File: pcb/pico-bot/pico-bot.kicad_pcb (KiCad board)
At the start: 2 copper layers, 101.6 x 54.6 mm, 62 parts, among them J1 Conn_01x02_Male, J2 Conn_01x06_Male, J3 Conn_01x06_Male, J4 Conn_01x06_Male, J5 Conn_01x06_Male, Q1 DMG2305UX, Q2 AOD417, SW1 SW_SPDT, SW2 SW_Push, SW3 SW_Push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

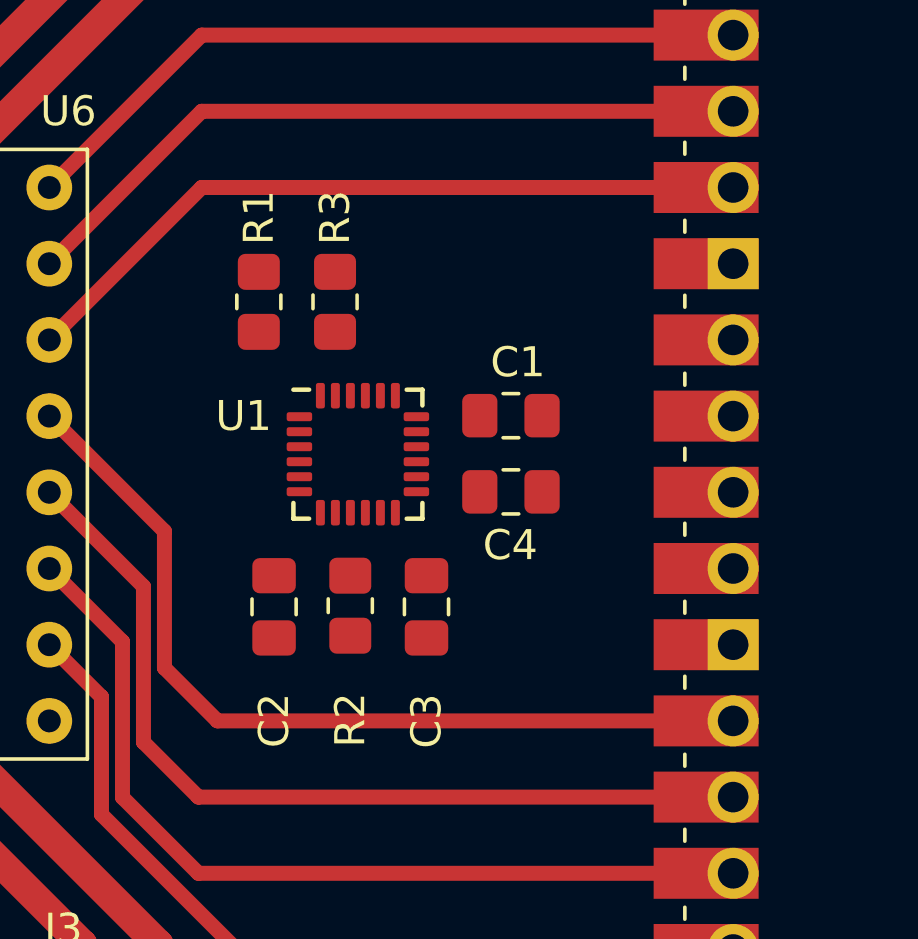
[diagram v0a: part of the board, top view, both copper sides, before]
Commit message: Center and route MPU-6050
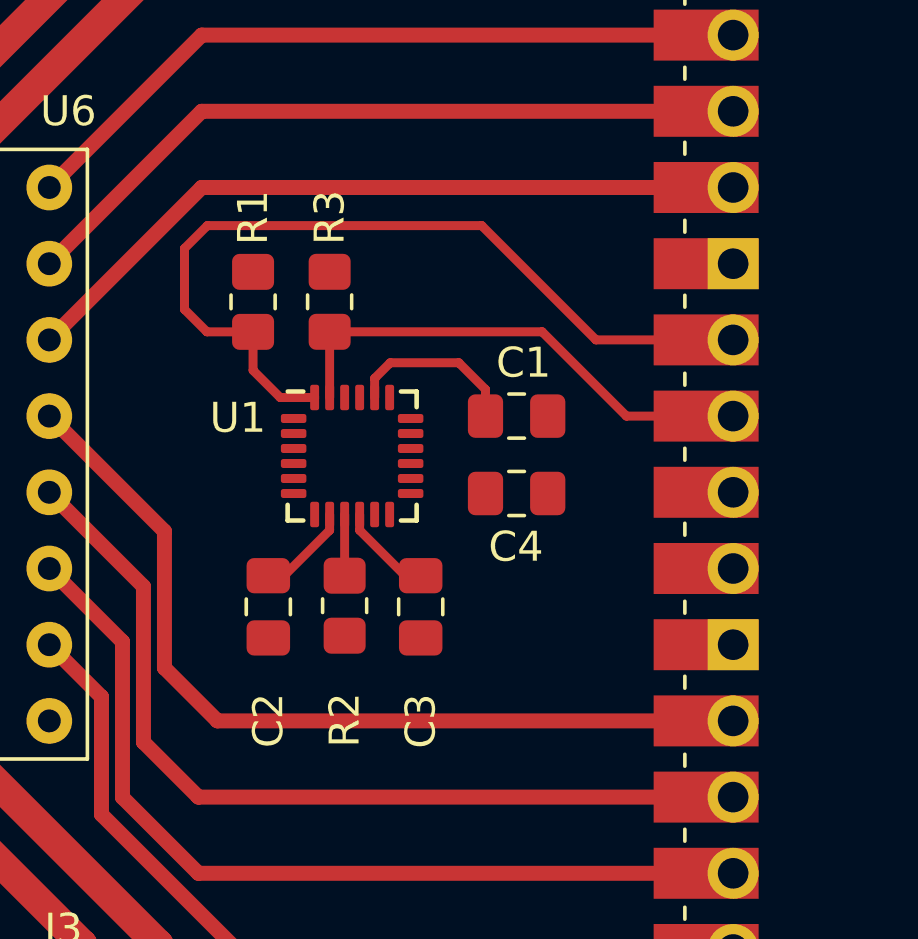
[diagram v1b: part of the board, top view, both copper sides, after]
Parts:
- moved U1 0.20 mm to (147.9, 93.8)
- moved C4 0.20 mm to (153.4, 95.0)
- moved C2 0.19 mm to (145.1, 98.8)
- moved C3 0.19 mm to (150.2, 98.8)
- moved R1 0.19 mm to (144.6, 88.7)
- moved C1 0.19 mm to (153.4, 92.5)
- moved R2 0.19 mm to (147.6, 98.8)
- moved R3 0.18 mm to (147.1, 88.7)
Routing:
- net /SDA: track 0.00 -> 28.5 mm
- net /SCL: track 0.02 -> 16.8 mm
- net Net-(C1-Pad2): track 0.00 -> 5.81 mm
- net +3V3: track 0.00 -> 3.20 mm
- net Net-(C3-Pad2): track 0.00 -> 3.19 mm
- net Net-(R2-Pad2): track 0.01 -> 2.04 mm

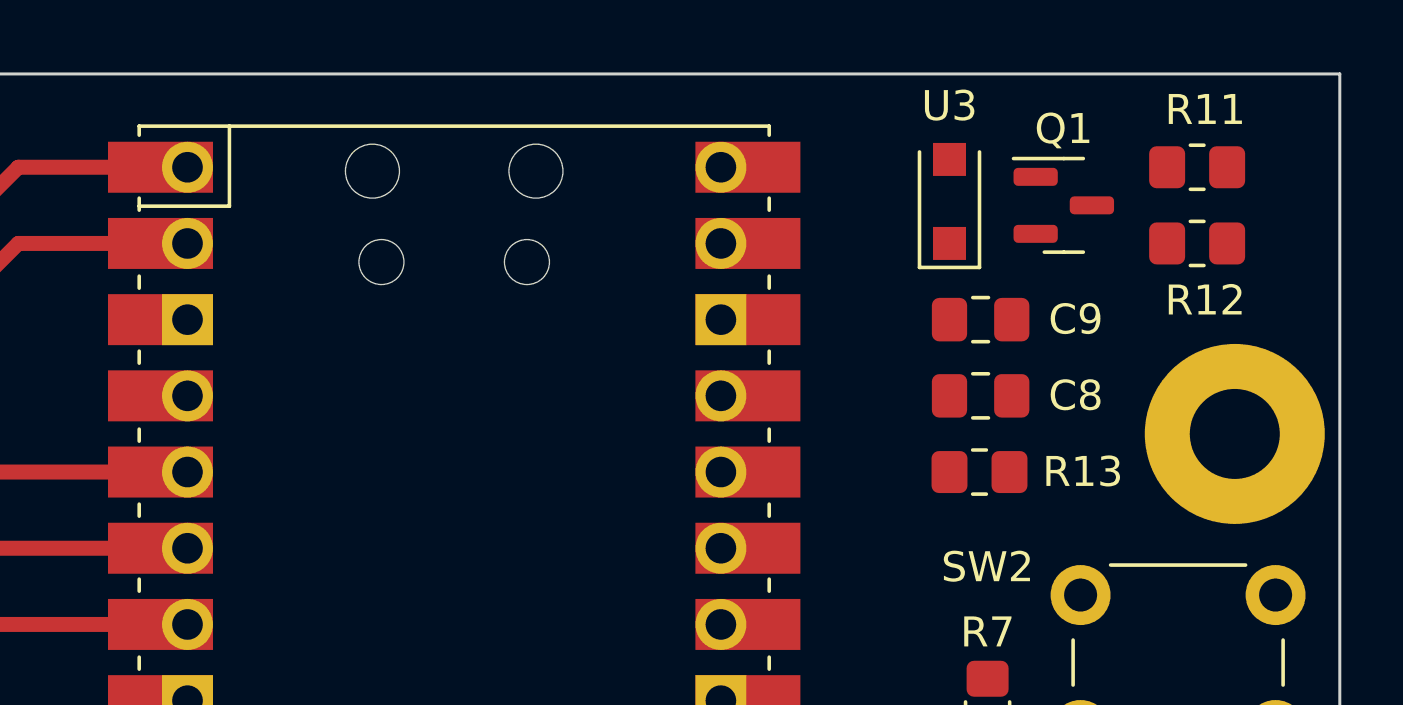
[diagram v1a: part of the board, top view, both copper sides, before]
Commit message: Route pico power select circuit
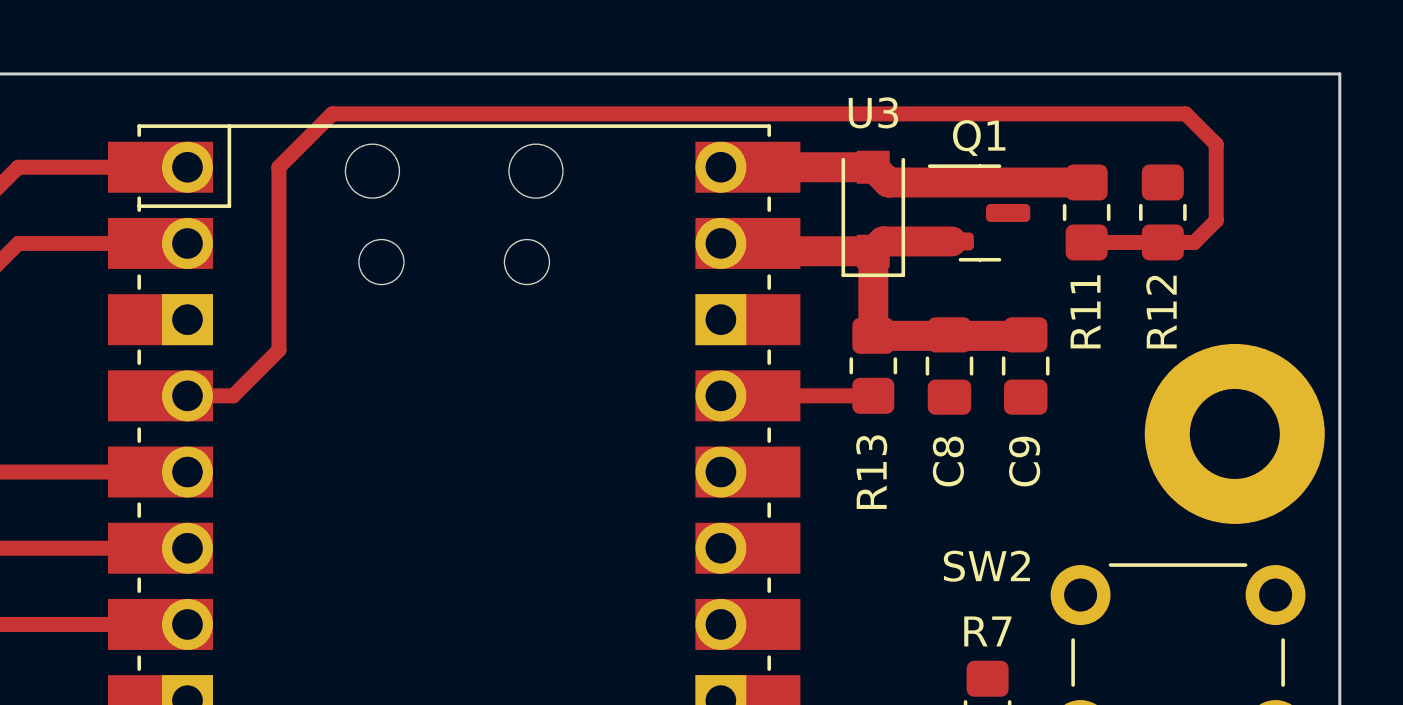
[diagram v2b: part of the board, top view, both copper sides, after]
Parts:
- moved R13 5.01 mm to (183.4, 76.2), turned to 90 degrees
- moved R11 3.98 mm to (190.6, 71.1), turned to 90 degrees
- moved Q1 2.81 mm to (187.0, 71.1)
- moved U3 2.55 mm to (183.4, 71.0)
- moved C9 2.16 mm to (188.5, 76.2), turned to 90 degrees
- moved R12 1.54 mm to (193.1, 71.1), turned to -90 degrees
- moved C8 1.44 mm to (186.0, 76.2), turned to 90 degrees
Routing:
- net /VBUS_IN: track 0.00 -> 49.3 mm
- net VSYS: track 0.00 -> 15.9 mm
- net VBUS: track 0.00 -> 12.4 mm
- net /3V3_EN: track 0.00 -> 5.08 mm

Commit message: Route all except power and ground
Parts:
- removed J5: Conn_01x06_Male, Connector_PinHeader_2.54mm:PinHeader_2x03_P2.54mm_Vertical
- J4: value Conn_01x06_Male -> Conn_01x08_Male; footprint Connector_PinHeader_2.54mm:PinHeader_2x03_P2.54mm_Vertical -> Connector_PinHeader_2.54mm:PinHeader_2x04_P2.54mm_Vertical
- R4: value 220R -> 10k
- R7: value 10k -> 220R
- moved R4 19.0 mm to (187.3, 85.8), turned to -90 degrees
- moved R7 15.1 mm to (185.5, 102.6), turned to 180 degrees
- moved SW2 7.91 mm to (196.9, 88.4), turned to 180 degrees
- moved R6 7.82 mm to (185.5, 105.2)
- moved R5 6.94 mm to (185.5, 97.5)
- moved TP1 2.29 mm to (100.9, 71.9)
- moved D1 1.91 mm to (193.6, 101.9), turned to 0 degrees
- moved J4 1.63 mm to (185.7, 110.2), turned to 0 degrees
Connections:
- J4 pad 2: /SPARE1 -> +3V3
- J4 pad 3: /SPARE2 -> /SPARE1
- J4 pad 4: /SPARE3 -> +3V3
- J4 pad 5: /SPARE4 -> /SPARE2
- J4 pad 6: /SPARE5 -> GND
- R4 pad 1: Net-(D1-Pad4) -> /MODE
- R4 pad 2: Net-(R4-Pad2) -> +3V3
- R5 pad 1: Net-(D1-Pad3) -> Net-(D1-Pad4)
- R6 pad 1: Net-(D1-Pad2) -> Net-(D1-Pad3)
- R7 pad 1: /MODE -> Net-(D1-Pad2)
- R7 pad 2: +3V3 -> Net-(R7-Pad2)
- U4 pad 12: /SPARE0 -> unconnected-(U4-Pad12)
- U4 pad 21: /SPARE5 -> /SPARE3
- U4 pad 22: /SPARE4 -> /SPARE2
- U4 pad 24: /SPARE3 -> /SPARE1
- U4 pad 25: /SPARE2 -> /SPARE0
- U4 pad 26: Net-(U4-Pad26) -> Net-(R6-Pad2)
- U4 pad 27: Net-(U4-Pad27) -> Net-(R7-Pad2)
- U4 pad 29: Net-(U4-Pad29) -> Net-(R5-Pad2)
- U4 pad 32: /SPARE1 -> unconnected-(U4-Pad32)
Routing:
- net /RESET: track 0.00 -> 19.7 mm
- net /MODE: track 0.00 -> 18.9 mm
- net Net-(D1-Pad4): track 0.00 -> 10.4 mm
- net Net-(D1-Pad3): track 0.00 -> 9.96 mm
- net /SPARE1: track 0.00 -> 8.42 mm
- net /SPARE0: track 0.00 -> 8.42 mm
- net /SPARE3: track 0.00 -> 7.37 mm
- net /SPARE2: track 0.00 -> 7.37 mm
- net Net-(R7-Pad2): track 0.00 -> 6.10 mm
- net Net-(R6-Pad2): track 0.00 -> 6.10 mm
- net Net-(R5-Pad2): track 0.00 -> 6.10 mm
- net Net-(D1-Pad2): track 0.00 -> 5.39 mm

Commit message: Add pours, pour currently broken
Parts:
- moved D3 23.2 mm to (131.6, 112.3), turned to 90 degrees
- moved R17 22.1 mm to (134.7, 112.3), turned to 90 degrees
- moved R4 4.31 mm to (183.4, 83.8), turned to 90 degrees
- moved R2 3.46 mm to (150.4, 100.9), turned to 180 degrees
- moved C17 1.42 mm to (122.5, 86.4), turned to -90 degrees
- moved C2 1.15 mm to (146.2, 98.7)
- moved J1 1.04 mm to (102.2, 102.4)
- moved C18 0.71 mm to (145.5, 72.4)
- moved C19 0.58 mm to (145.5, 115.3)
- moved C4 0.51 mm to (152.9, 95.0)
- moved R1 0.41 mm to (145.0, 88.8)
- moved C3 0.39 mm to (150.5, 98.6), turned to 180 degrees
- moved C15 0.16 mm to (126.8, 115.6)
- moved R3 0.14 mm to (147.1, 88.8)
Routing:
- net /VBAT_MEASURE: track 0.55 -> 78.1 mm
- net GND: track 0.00 -> 45.2 mm, vias 0 -> 28
- net /INT: track 0.00 -> 12.4 mm
- net VBAT: track 43.1 -> 51.8 mm
- net Net-(R2-Pad2): track 2.04 -> 6.36 mm
- net +3V3: track 3.20 -> 0.00 mm
- net /STDBY: track 29.7 -> 31.4 mm
- net /SDA: track 28.5 -> 27.4 mm
- net Net-(C3-Pad2): track 3.19 -> 3.80 mm
- net /MODE: track 18.9 -> 18.4 mm
- added copper zone on F.Cu, net +3V3
- added copper zone on B.Cu, net GND
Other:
- outline, holes or cut-outs redrawn
- board text added: "+"
- board text added: "-"
- board text added: "MODE"
- board text added: "OFF"
- board text added: "ON"
- board text added: "RESET"

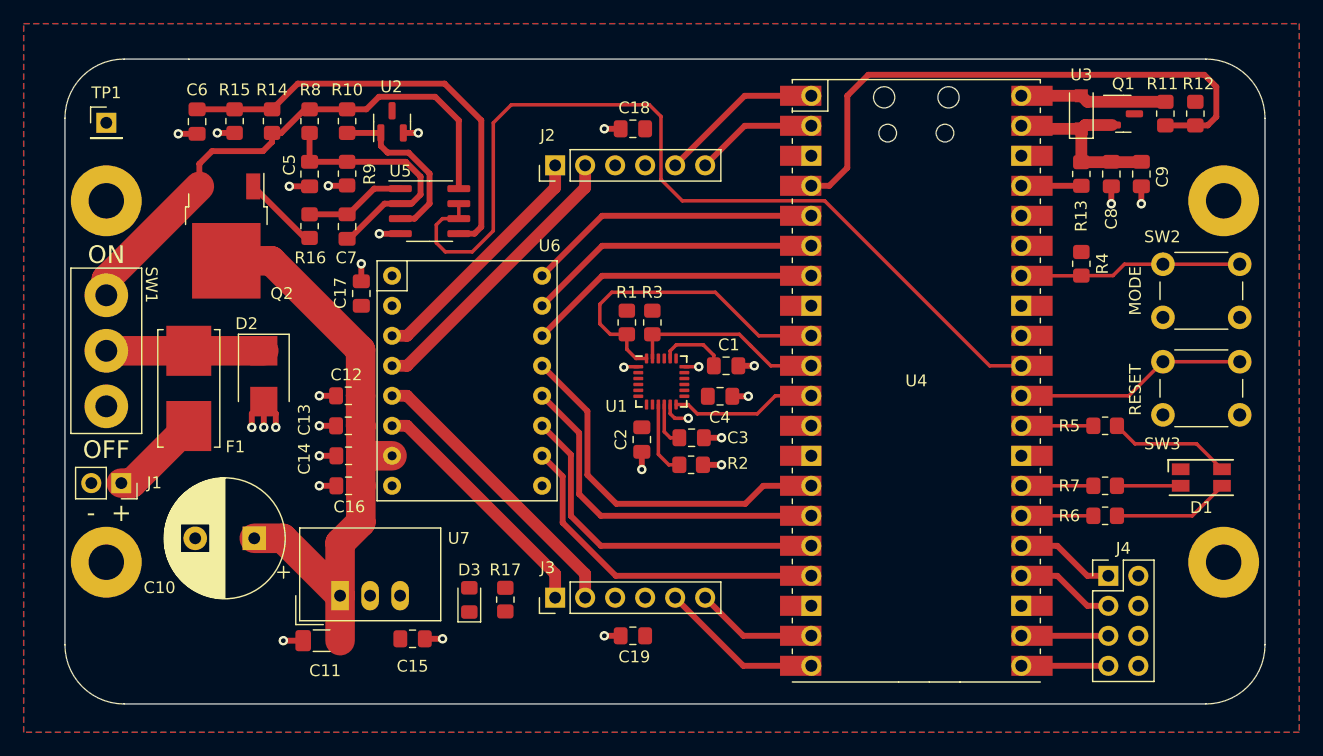
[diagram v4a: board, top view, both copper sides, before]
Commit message: Update pour clearance and repour, now all nets are connected
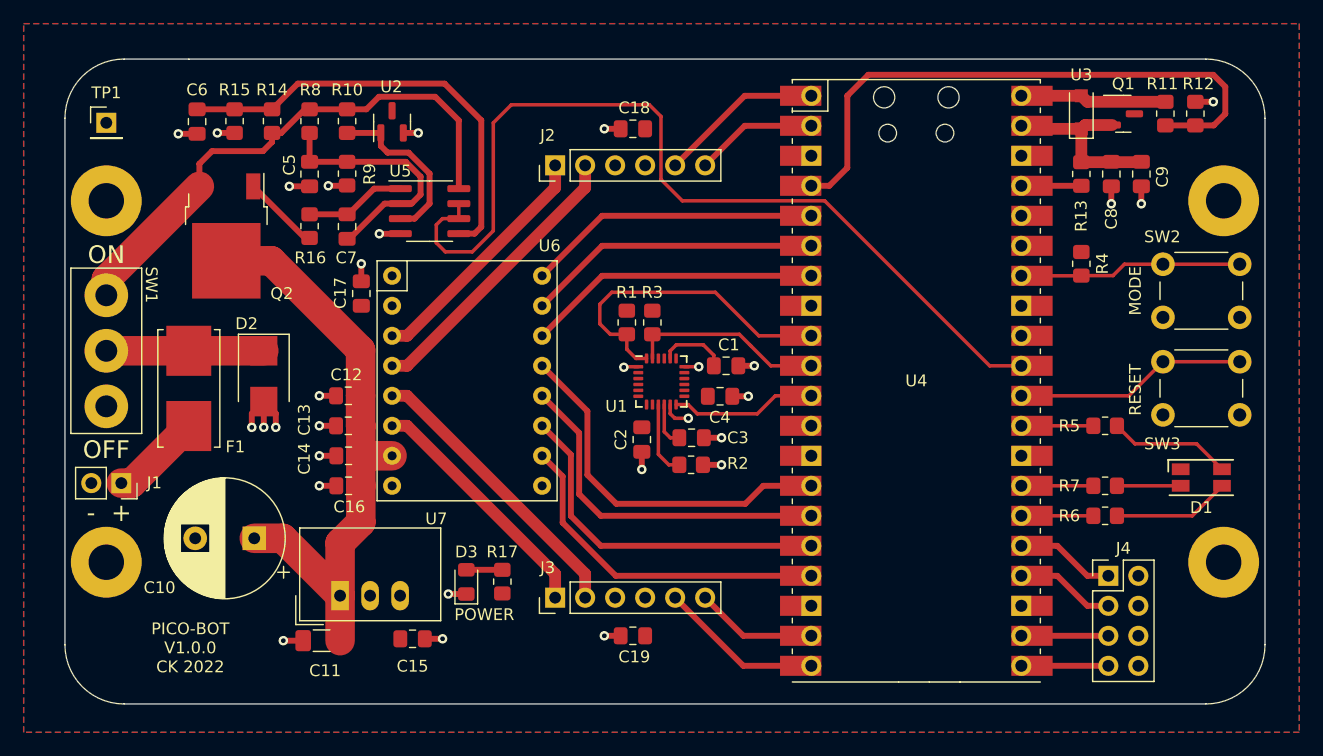
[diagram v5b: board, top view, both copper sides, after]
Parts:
- moved D3 1.55 mm to (131.4, 110.8)
- moved R17 1.55 mm to (134.4, 110.7)
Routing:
- net GND: track 45.2 -> 48.3 mm, vias 28 -> 30
- net Net-(D3-Pad2): track 0.00 -> 3.05 mm
- net /VBUS_IN: track 49.3 -> 50.7 mm
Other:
- board text added: "PICO-BOT V1.0.0 CK 2022"
- board text added: "POWER"

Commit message: Address DRC warnings
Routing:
- net /VBAT_MEASURE: track 78.1 -> 77.6 mm
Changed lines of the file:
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@@
   (segment (start 143.064 72.404) (end 144.445 72.404) (width 0.5) (layer "F.Cu") (net 1))
   (segment (start 119.696 77.23) (end 121.255 77.23) (width 0.5) (layer "F.Cu") (net 1))
-  (segment (start 121.255 77.23) (end 121.285 77.2) (width 0.5) (layer "F.Cu") (net 1))
   (segment (start 185.99 78.754) (end 185.99 77.273) (width 0.5) (layer "F.Cu") (net 1))
   (segment (start 114.235 97.682) (end 114.235 95.5) (width 0.5) (layer "F.Cu") (net 1))
   (segment (start 106.996 72.83) (end 108.585 72.83) (width 0.5) (layer "F.Cu") (net 1))
   (segment (start 148.64 95.75) (end 148.64 96.522) (width 0.3) (layer "F.Cu") (net 1))
-  (segment (start 121.21 77.275) (end 121.285 77.2) (width 0.5) (layer "F.Cu") (net 1))
   (segment (start 151.065 92.55) (end 149.84 92.55) (width 0.3) (layer "F.Cu") (net 1))
   (segment (start 115.251 97.682) (end 115.251 96.516) (width 0.5) (layer "F.Cu") (net 1))
@@
   (segment (start 132.08 81.28) (end 132.65 80.71) (width 0.5) (layer "F.Cu") (net 6))
   (segment (start 132.65 71.69) (end 129.54 68.58) (width 0.5) (layer "F.Cu") (net 6))
-  (segment (start 121.285 79.645) (end 121.396 79.645) (width 0.5) (layer "F.Cu") (net 7))
-  (segment (start 121.285 79.645) (end 121.285 79.375) (width 0.5) (layer "F.Cu") (net 7))
   (segment (start 123.571 77.47) (end 125.795 77.47) (width 0.5) (layer "F.Cu") (net 7))
   (segment (start 121.396 79.645) (end 123.571 77.47) (width 0.5) (layer "F.Cu") (net 7))
@@
   (segment (start 131.888 82.818) (end 133.666 81.04) (width 0.3) (layer "F.Cu") (net 44))
   (segment (start 149.668 78.5) (end 161.719022 78.5) (width 0.3) (layer "F.Cu") (net 44))
-  (segment (start 130.68 80.01) (end 131.232849 80.01) (width 0.5) (layer "F.Cu") (net 44))
   (segment (start 129.602 82.818) (end 131.888 82.818) (width 0.3) (layer "F.Cu") (net 44))
   (segment (start 133.666 81.04) (end 133.666 71.896) (width 0.3) (layer "F.Cu") (net 44))

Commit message: Update silkscreen
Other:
- board text added: "0"
- board text added: "1"
- board text added: "2"
- board text added: "3"
- board text added: "USB"
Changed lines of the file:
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@@
     (property "Sheetname" "")
     (attr smd)
-    (fp_text reference "U3" (at 3.175 0) (layer "F.SilkS")
+    (fp_text reference "U3" (at 2.924 0) (layer "F.SilkS")
       (effects (font (size 1 1) (thickness 0.15)))
     )
@@
     (effects (font (size 1 1) (thickness 0.15)))
   )
-  (gr_text "ON" (at 100.9 83.072) (layer "F.SilkS")
-    (effects (font (size 1.5 1.5) (thickness 0.3)))
-  )
-  (gr_text "-" (at 99.6 104.916) (layer "F.SilkS")
-    (effects (font (size 1.5 1.5) (thickness 0.3)))
+  (gr_text "1" (at 183.704 112.79) (layer "F.SilkS")
+    (effects (font (size 1 1) (thickness 0.15)))
+  )
+  (gr_text "ON" (at 100.9 83.326) (layer "F.SilkS")
+    (effects (font (size 1 1) (thickness 0.15)))
+  )
+  (gr_text "-" (at 190.562 115.33) (layer "F.SilkS")
+    (effects (font (size 1 1) (thickness 0.15)))
+  )
+  (gr_text "-" (at 99.6 104.662) (layer "F.SilkS")
+    (effects (font (size 1 1) (thickness 0.15)))
+  )
+  (gr_text "-" (at 190.562 117.87) (layer "F.SilkS")
+    (effects (font (size 1 1) (thickness 0.15)))
   )
   (gr_text "POWER" (at 132.904 113.536) (layer "F.SilkS")
@@
     (effects (font (size 1 1) (thickness 0.15)))
   )
-  (gr_text "OFF" (at 100.9 99.582) (layer "F.SilkS")
-    (effects (font (size 1.5 1.5) (thickness 0.3)))
+  (gr_text "OFF" (at 100.9 99.074) (layer "F.SilkS")
+    (effects (font (size 1 1) (thickness 0.15)))
+  )
+  (gr_text "3" (at 183.704 117.87) (layer "F.SilkS")
+    (effects (font (size 1 1) (thickness 0.15)))
+  )
+  (gr_text "+" (at 190.562 110.25) (layer "F.SilkS")
+    (effects (font (size 1 1) (thickness 0.15)))
+  )
+  (gr_text "0" (at 183.704 110.25) (layer "F.SilkS")
+    (effects (font (size 1 1) (thickness 0.15)))
   )
   (gr_text "MODE" (at 188.022 86.12 90) (layer "F.SilkS")
     (effects (font (size 1 1) (thickness 0.15)))
   )
-  (gr_text "+" (at 102.17 104.916) (layer "F.SilkS")
-    (effects (font (size 1.5 1.5) (thickness 0.3)))
+  (gr_text "2" (at 183.704 115.33) (layer "F.SilkS")
+    (effects (font (size 1 1) (thickness 0.15)))
+  )
+  (gr_text "USB" (at 169.48 67.578) (layer "F.SilkS")
+    (effects (font (size 1 1) (thickness 0.15)))
+  )
+  (gr_text "+" (at 190.562 112.536) (layer "F.SilkS")
+    (effects (font (size 1 1) (thickness 0.15)))
+  )
+  (gr_text "+" (at 102.17 104.662) (layer "F.SilkS")
+    (effects (font (size 1 1) (thickness 0.15)))
   )
   (segment (start 129.856 111.792) (end 131.38 111.792) (width 0.5) (layer "F.Cu") (net 1))
